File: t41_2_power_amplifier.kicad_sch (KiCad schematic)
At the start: 83 parts, among them J1 5-1814832-1, J2 5-1814832-1, J3 B2B-XH-A_LF__SN_, J5 Screw_Terminal_01x02, Q1 Q_NMOS_GSD, Q2 Q_NPN_BCE, Q3 Q_NMOS_GSD, Q4 Q_NPN_BCE, Q5 Q_NPN_BEC, Q7 Q_NPN_BEC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

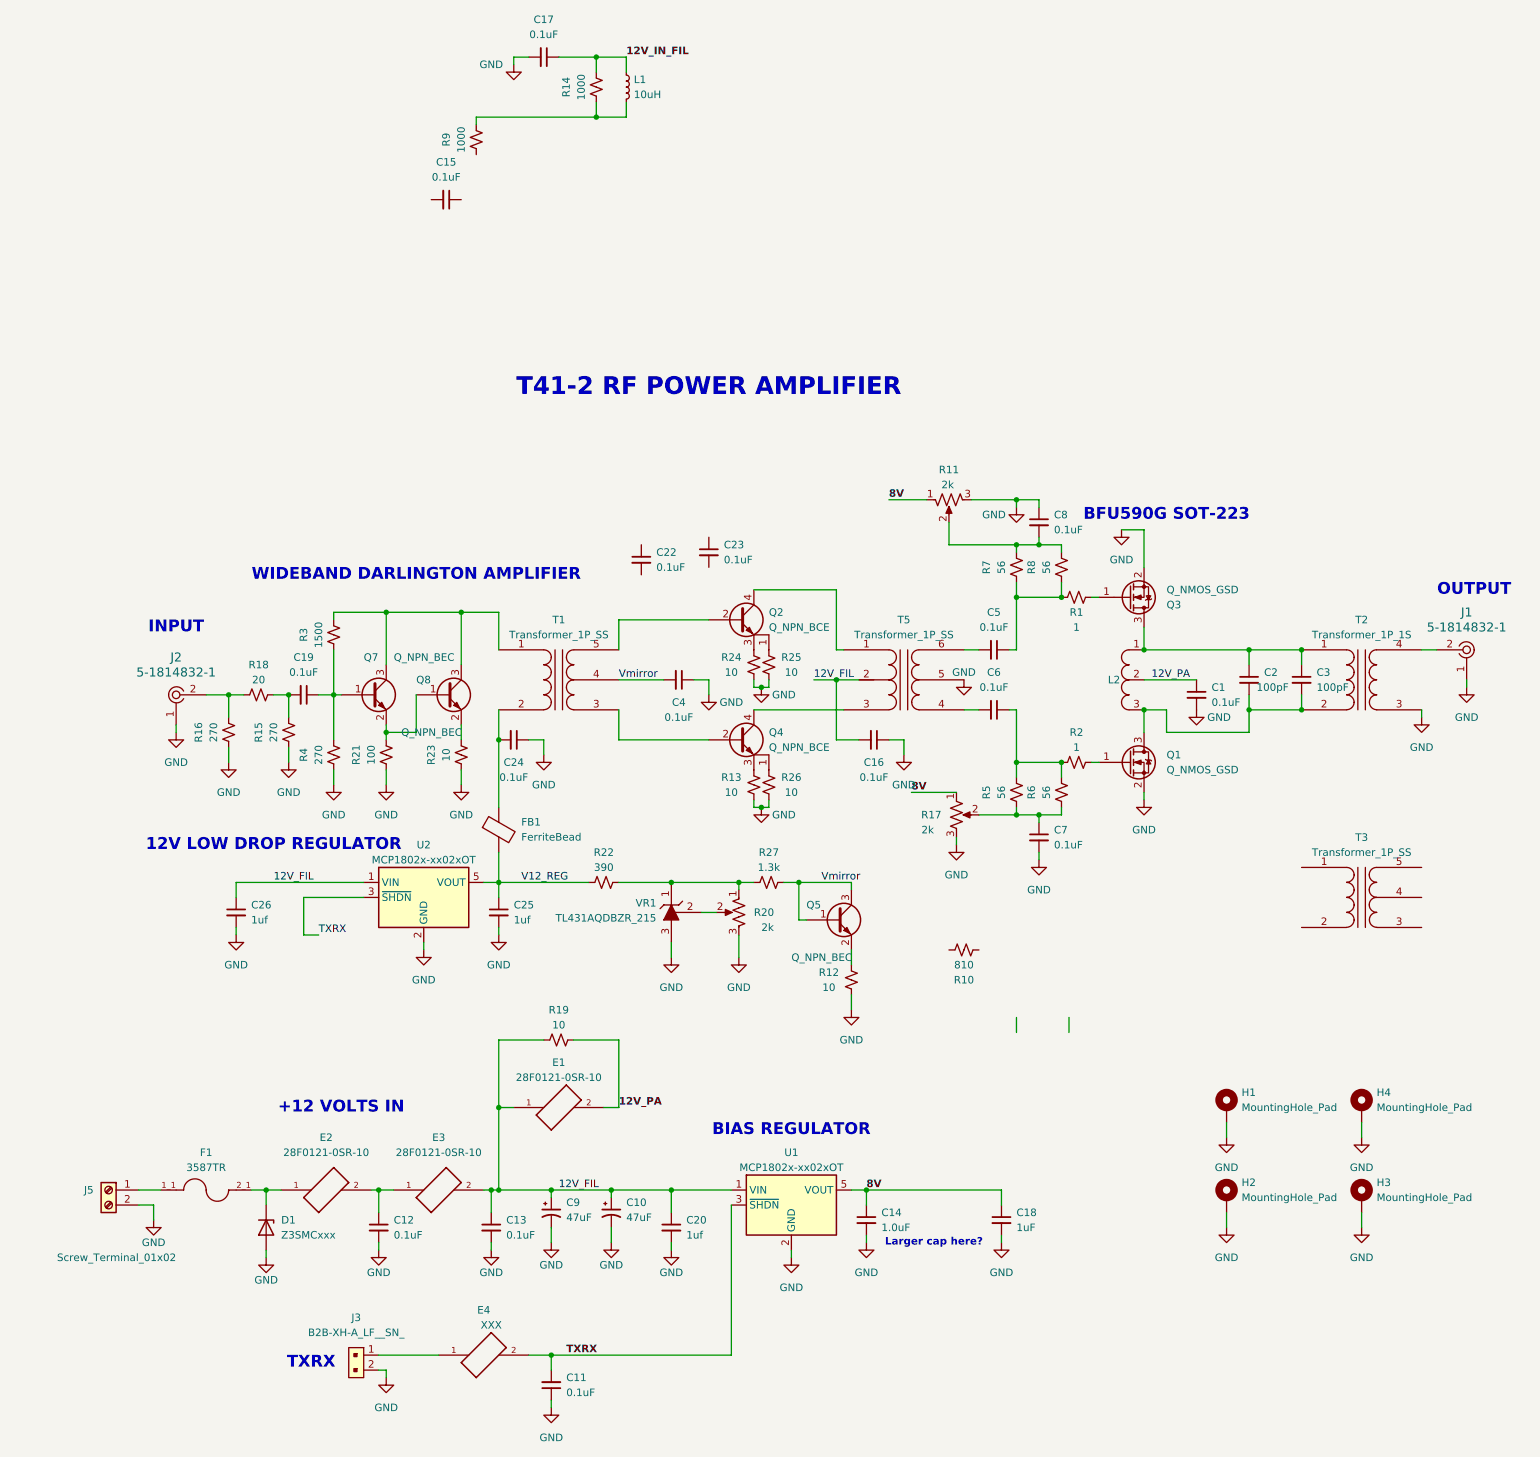
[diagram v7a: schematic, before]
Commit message: Power Amplifier module ready for fab.
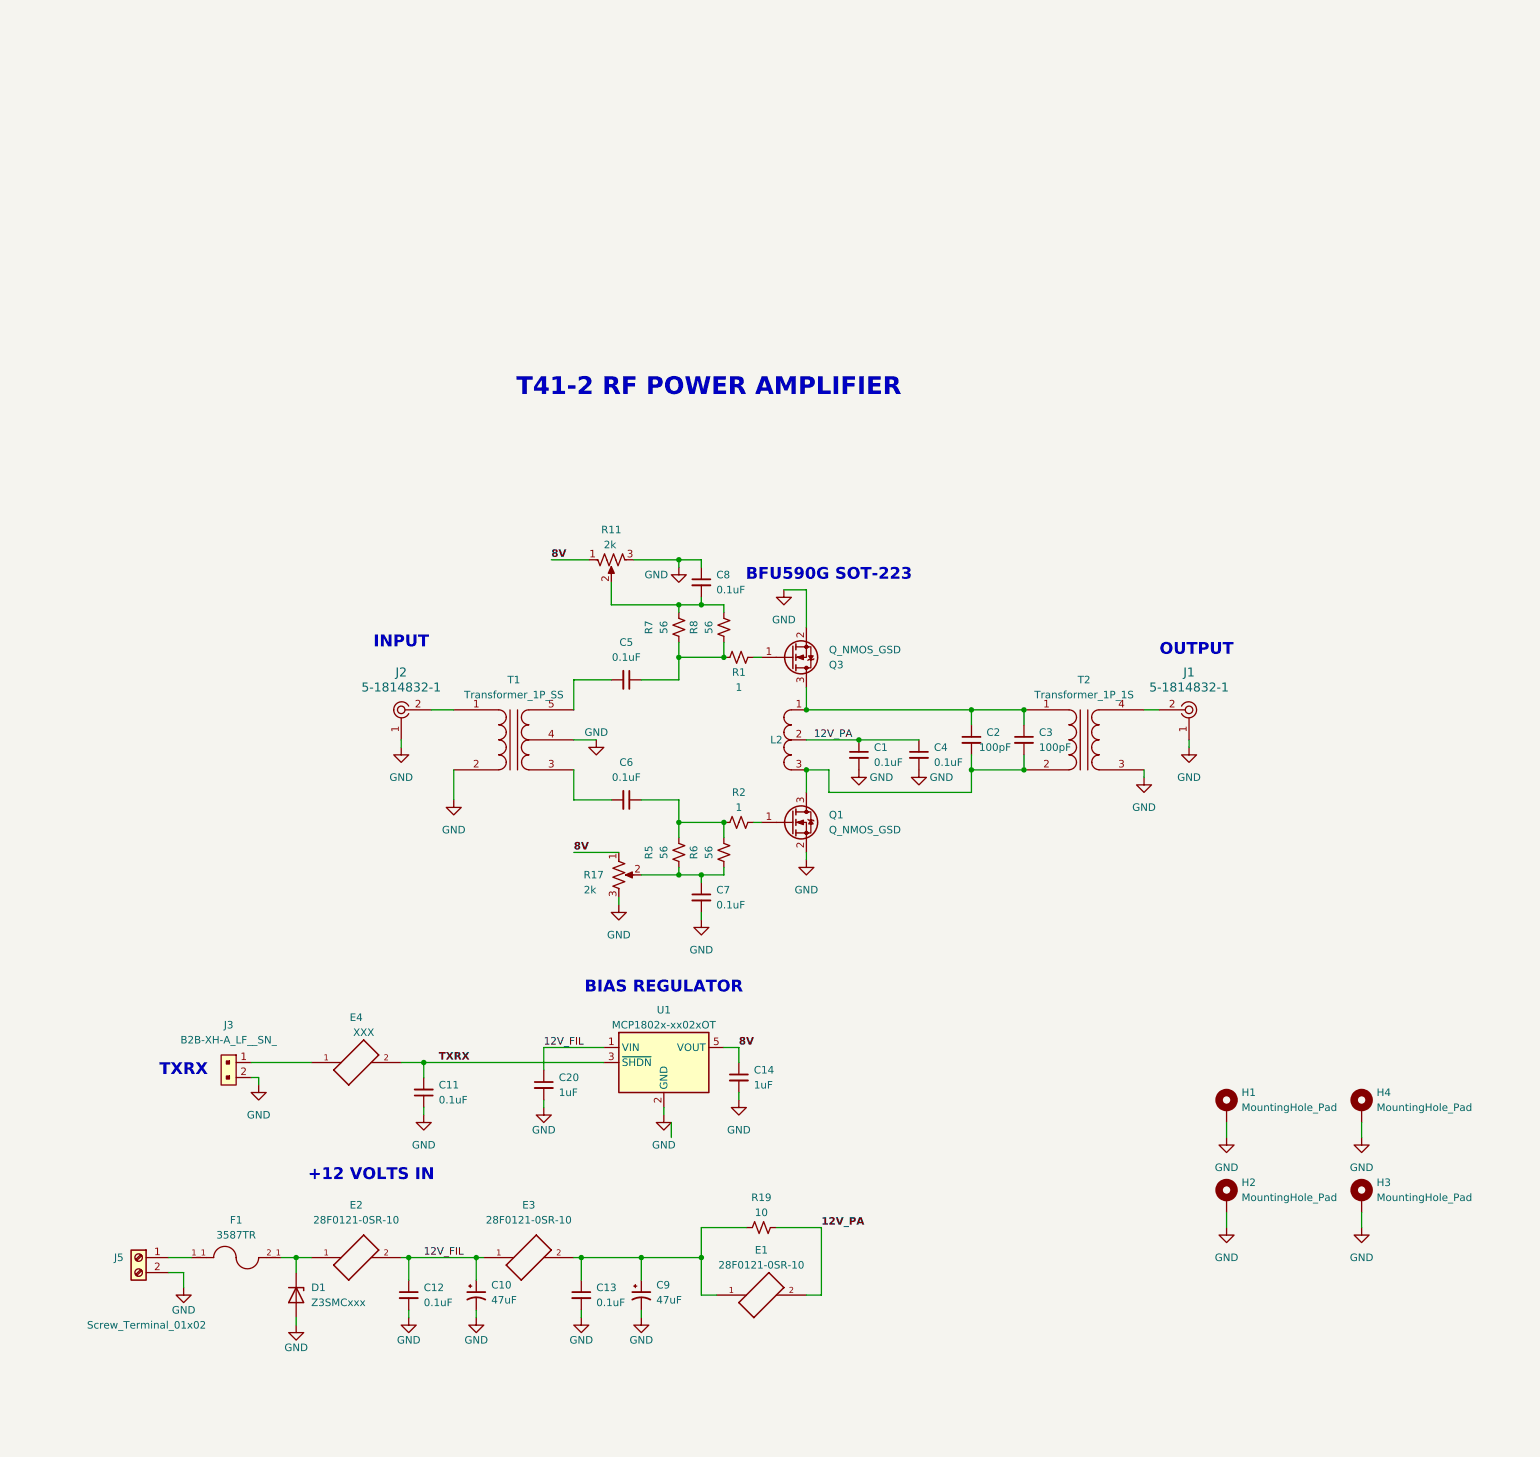
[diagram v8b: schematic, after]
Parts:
- removed C15, C16, C17, C19, C22, C23, C24: 0.1uF, Capacitor_SMD:C_1206_3216Metric, symbol Device:C_Small
- removed C18: 1uF, Capacitor_SMD:C_1206_3216Metric, symbol Device:C_Small
- removed C25, C26: 1uf, Capacitor_SMD:C_1206_3216Metric, symbol Device:C_Small
- removed FB1: FerriteBead, symbol Device:FerriteBead
- removed L1: 10uH, Inductor_SMD:L_1210_3225Metric, symbol Device:L_Small
- removed Q2, Q4: Q_NPN_BCE, Package_TO_SOT_SMD:SOT-223, symbol Device:Q_NPN_BCE
- removed Q5, Q7, Q8: Q_NPN_BEC, Package_TO_SOT_SMD:SOT-23-3, symbol Device:Q_NPN_BEC
- removed R10: 810, Resistor_SMD:R_1206_3216Metric, symbol Device:R_Small_US
- removed R12, R13, R23, R24, R25, R26: 10, Resistor_SMD:R_1206_3216Metric, symbol Device:R_Small_US
- removed R14, R9: 1000, Resistor_SMD:R_1206_3216Metric, symbol Device:R_Small_US
- removed R15, R16, R4: 270, Resistor_SMD:R_1206_3216Metric, symbol Device:R_Small_US
- removed R18: 20, Resistor_SMD:R_1206_3216Metric, symbol Device:R_Small_US
- removed R20: 2k, Potentiometer_THT:Potentiometer_Bourns_3296W_Vertical, symbol Device:R_Potentiometer_US
- removed R21: 100, Resistor_SMD:R_1206_3216Metric, symbol Device:R_Small_US
- removed R22: 390, Resistor_SMD:R_1206_3216Metric, symbol Device:R_Small_US
- removed R27: 1.3k, Resistor_SMD:R_1206_3216Metric, symbol Device:R_Small_US
- removed R3: 1500, Resistor_SMD:R_1206_3216Metric, symbol Device:R_Small_US
- removed T3: Transformer_1P_SS, Binocular_Core:BN-43-302, symbol Device:Transformer_1P_SS
- removed T5: Transformer_1P_SS, symbol Transformer_Double_Tapped:Transformer_1P_SS
- removed U2: MCP1802x-xx02xOT, Package_TO_SOT_SMD:SOT-23-5, symbol Regulator_Linear:MCP1802x-xx02xOT
- removed VR1: TL431AQDBZR_215, digikey-footprints:SOT-23-3, symbol dk_PMIC-Voltage-Reference:TL431AQDBZR_215
- C14: value 1.0uF -> 1uF
- C20: value 1uf -> 1uF
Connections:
- net Vmirror is gone; now on net GND: C4.2, T1.4 (SC)
- net 12V_FIL: now also C12.1, E2.2, E3.1; no longer C13.1, C9.1, E1.1, E3.2, R19.1
- net 12V_PA: now also C4.1
- net GND: now also T1.2 (AB); no longer C4.1
- net at T1.1 (AA): now also J2.2
- net at T1.3 (SA): now also C6.2
- net at T1.5 (SB): now also C5.2
- new net: C13.1, C9.1, E1.1, E3.2, R19.1
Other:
- note removed: "12V LOW DROP REGULATOR"
- note removed: "Larger cap here?"
- note removed: "WIDEBAND DARLINGTON AMPLIFIER"
- moved on the sheet: C1, C10, C11, C12, C13, C14, C2, C20, C3, C5, C6, C7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
